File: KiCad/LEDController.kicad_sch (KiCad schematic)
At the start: 47 parts, among them J1 Conn_01x05, J2 UART, J3 JTAG, J5 USB_C_Receptacle_USB2.0_16P, J6 Conn_01x03, J7 VDD, J8 GND, J9 Conn_01x14, Q1 IRLZ44N, Q2 IRLZ44N, Q3 IRLZ44N, Q4 IRLZ44N, SW1 BOOT, SW2 EN, U2 ESP32-S3-WROOM-2, U3 TPS54202DDC

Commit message: .
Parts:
- C12, C14, C15, C5: footprint Capacitor_SMD:C_1210_3225Metric_Pad1.33x2.70mm_HandSolder -> Capacitor_SMD:C_0805_2012Metric_Pad1.18x1.45mm_HandSolder; LCSC (none) -> C33546007
- D1: footprint (none) -> LED_SMD:LED_0603_1608Metric_Pad1.05x0.95mm_HandSolder
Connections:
- net GPIO.6: now also U2.6 (GPIO6/TOUCH6/ADC1_CH5)
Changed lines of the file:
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@@
 		)
 	)
+	(global_label "GPIO.6"
+		(shape input)
+		(at 125.73 146.05 0)
+		(fields_autoplaced yes)
+		(effects
+			(font
+				(size 1.27 1.27)
+			)
+			(justify left)
+		)
+		(property "Intersheetrefs" "${INTERSHEET_REFS}"
+			(at 135.0048 146.05 0)
+			(effects
+				(font
+					(size 1.27 1.27)
+				)
+				(justify left)
+				(hide yes)
+			)
+		)
+	)
 	(global_label "UART.RX"
 		(shape input)
@@
 			)
 		)
-		(property "Footprint" "Capacitor_SMD:C_1210_3225Metric_Pad1.33x2.70mm_HandSolder"
+		(property "Footprint" "Capacitor_SMD:C_0805_2012Metric_Pad1.18x1.45mm_HandSolder"
 			(at 266.7 137.16 0)
 			(effects
@@
 			)
 		)
+		(property "LCSC" "C33546007"
+			(at 266.7 137.16 0)
+			(effects
+				(font
+					(size 1.27 1.27)
+				)
+				(hide yes)
+			)
+		)
 		(pin "1"
 		)
@@
 			)
 		)
-		(property "Footprint" "Capacitor_SMD:C_1210_3225Metric_Pad1.33x2.70mm_HandSolder"
+		(property "Footprint" "Capacitor_SMD:C_0805_2012Metric_Pad1.18x1.45mm_HandSolder"
 			(at 204.47 140.97 0)
 			(effects
@@
 			)
 		)
+		(property "LCSC" "C33546007"
+			(at 204.47 140.97 0)
+			(effects
+				(font
+					(size 1.27 1.27)
+				)
+				(hide yes)
+			)
+		)
 		(pin "1"
 		)
@@
 			)
 		)
-		(property "Footprint" "Capacitor_SMD:C_1210_3225Metric_Pad1.33x2.70mm_HandSolder"
+		(property "Footprint" "Capacitor_SMD:C_0805_2012Metric_Pad1.18x1.45mm_HandSolder"
 			(at 274.32 137.16 0)
 			(effects
@@
 			)
 		)
+		(property "LCSC" "C33546007"
+			(at 274.32 137.16 0)
+			(effects
+				(font
+					(size 1.27 1.27)
+				)
+				(hide yes)
+			)
+		)
 		(pin "1"
 		)
@@
 			)
 		)
-		(property "Footprint" "Capacitor_SMD:C_1210_3225Metric_Pad1.33x2.70mm_HandSolder"
+		(property "Footprint" "Capacitor_SMD:C_0805_2012Metric_Pad1.18x1.45mm_HandSolder"
 			(at 24.13 119.38 0)
 			(effects
@@
 			)
 		)
+		(property "LCSC" "C33546007"
+			(at 24.13 119.38 0)
+			(effects
+				(font
+					(size 1.27 1.27)
+				)
+				(hide yes)
+			)
+		)
 		(pin "2"
 		)
@@
 			)
 		)
-		(property "Footprint" ""
+		(property "Footprint" "LED_SMD:LED_0603_1608Metric_Pad1.05x0.95mm_HandSolder"
 			(at 128.27 90.17 0)
 			(effects

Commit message: .
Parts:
- added C6: 10u, Capacitor_SMD:C_0805_2012Metric_Pad1.18x1.45mm_HandSolder, symbol Device:C_Small
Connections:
- net +3.3V: now also C6.1
- net GND: now also C6.2
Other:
- moved on the sheet: C14, C15, J5, R12, R13, R14

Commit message: jlcpcb order
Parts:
- removed R10: 100k, Resistor_SMD:R_0805_2012Metric_Pad1.20x1.40mm_HandSolder, symbol Device:R_Small
- removed R11: 21.7995k, Resistor_SMD:R_0805_2012Metric_Pad1.20x1.40mm_HandSolder, symbol Device:R_Small
- added C12: 10u, Capacitor_SMD:C_0805_2012Metric_Pad1.18x1.45mm_HandSolder, symbol Device:C_Small
- C1, C2, C3: LCSC (none) -> C5137467
- C4: value 22u -> 10u; LCSC (none) -> C33546007
- C6: renamed from C10; LCSC (none) -> C5137467
- C7: renamed from C11; LCSC (none) -> C5137467
- L1: renamed from L2; value 15u -> 10u; LCSC (none) -> C5349663
- U1: renamed from U3; LCSC (none) -> C191884
- renumbered C14 to C10, C15 to C11, C12 to C8, C6 to C9, J2 to J1, J7 to J2, J8 to J3, J1 to J4, J6 to J5, J5 to J6, J9 to J7, J3 to J8, R12 to R10, R13 to R11, R14 to R12, R9 to R7, R7 to R9
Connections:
- net +3.3V: now also C12.1
- net GND: now also C12.2
- net GPIO.48: no longer names the net of U2.25 (GPIO48/SPICLK_N/SUBSPICLK_N_DIFF)
- no-connect marks 9 -> 11
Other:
- note added: "IRLB8721"
- note added: "verbessern"
- moved on the sheet: C10, C11, C3, C6, C7, C8, C9, L1, R10, R11, R12, U1

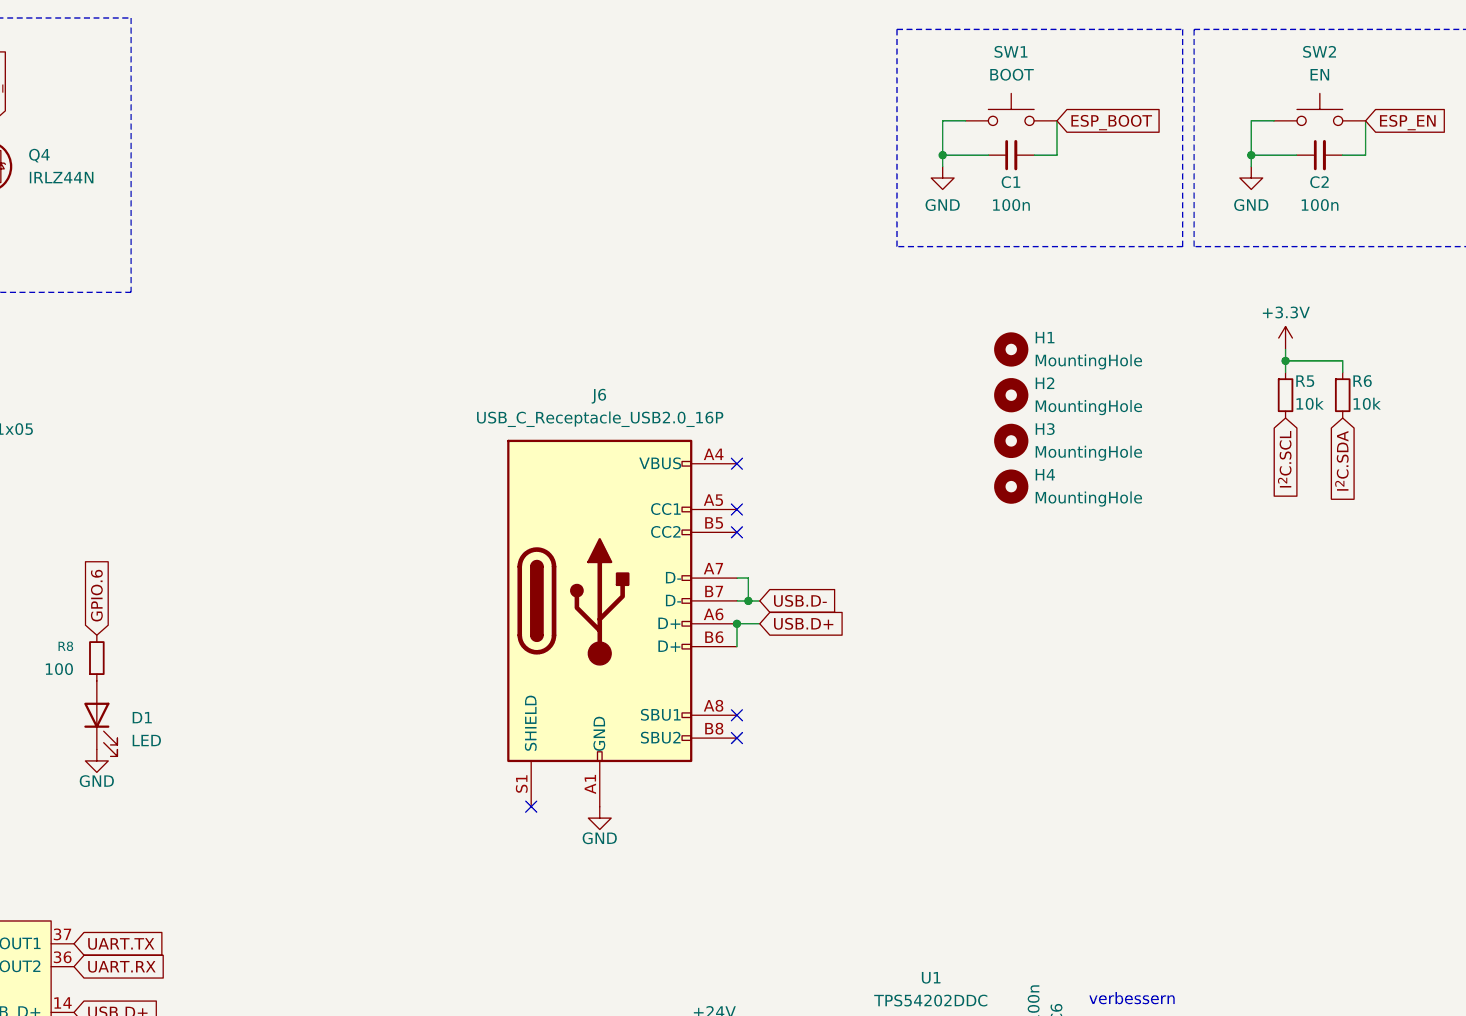
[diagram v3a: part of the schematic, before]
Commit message: add mains power
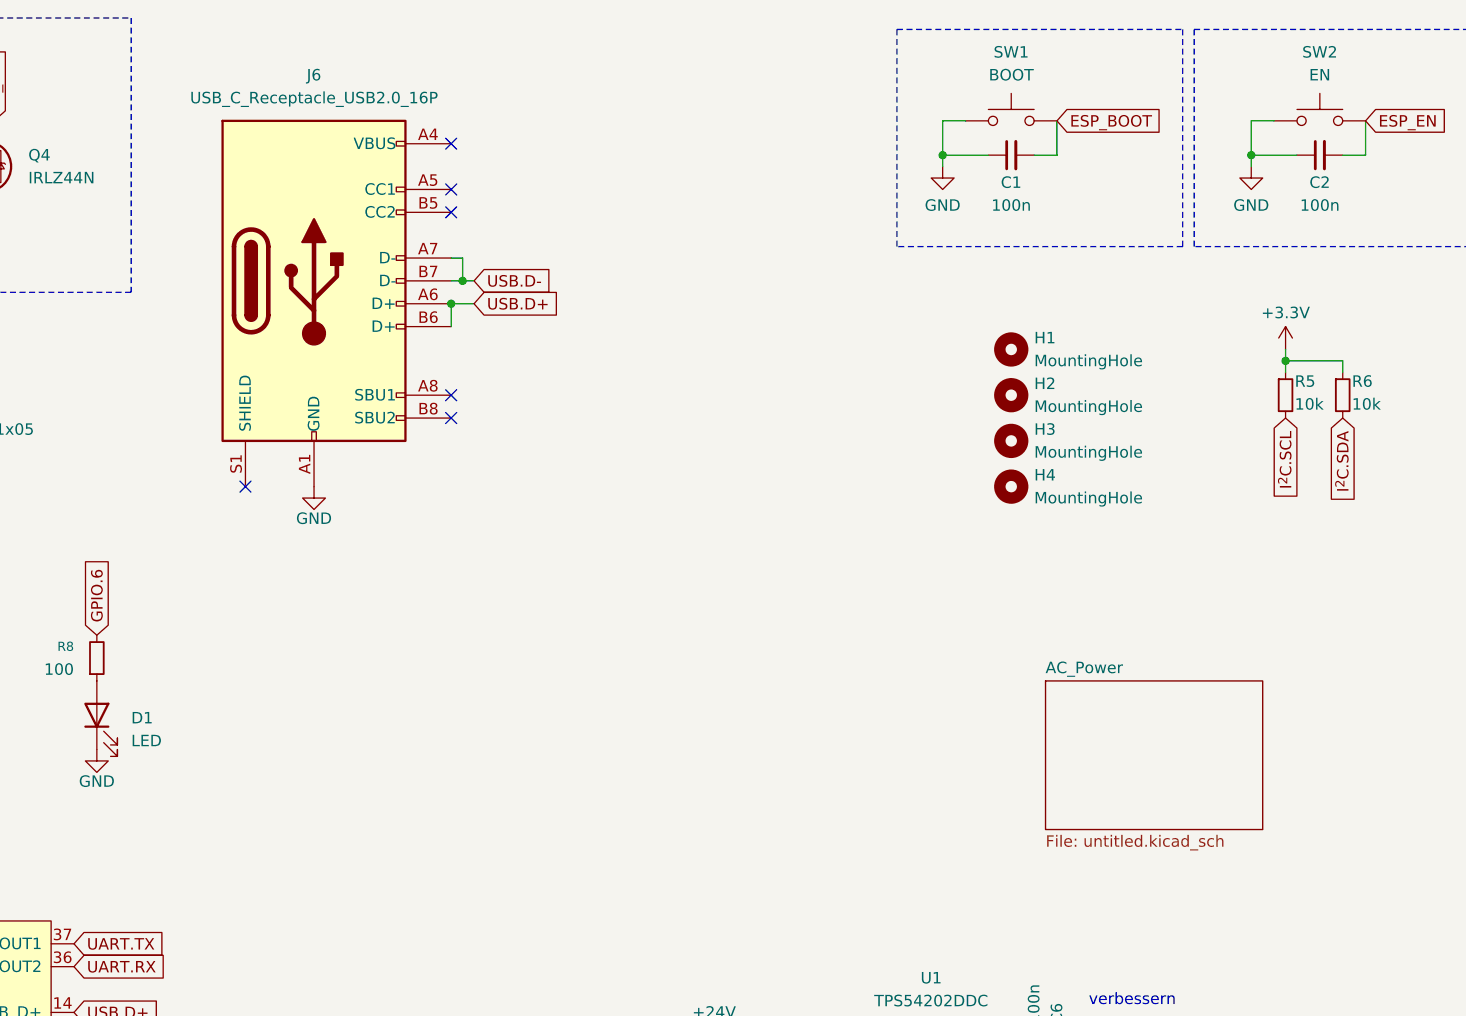
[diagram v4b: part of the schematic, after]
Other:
- added sheet AC_Power (untitled.kicad_sch)
- moved on the sheet: J6
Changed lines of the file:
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@@
 	)
 	(junction
-		(at 199.39 80.01)
+		(at 167.64 44.45)
 		(diameter 0)
 		(color 0 0 0 0)
@@
 	)
 	(junction
-		(at 200.66 77.47)
+		(at 168.91 41.91)
 		(diameter 0)
 		(color 0 0 0 0)
@@
 	)
 	(no_connect
-		(at 199.39 62.23)
+		(at 167.64 26.67)
 	)
 	(no_connect
-		(at 199.39 90.17)
+		(at 167.64 54.61)
 	)
 	(no_connect
@@
 	)
 	(no_connect
-		(at 199.39 67.31)
+		(at 167.64 31.75)
 	)
 	(no_connect
-		(at 199.39 92.71)
+		(at 167.64 57.15)
 	)
 	(no_connect
@@
 	)
 	(no_connect
-		(at 199.39 69.85)
+		(at 167.64 34.29)
 	)
 	(no_connect
-		(at 176.53 100.33)
+		(at 144.78 64.77)
 	)
 	(wire
@@
 	(wire
 		(pts
-			(xy 199.39 77.47) (xy 200.66 77.47)
+			(xy 167.64 41.91) (xy 168.91 41.91)
 		)
 		(stroke
@@
 	(wire
 		(pts
-			(xy 199.39 80.01) (xy 201.93 80.01)
+			(xy 167.64 44.45) (xy 170.18 44.45)
 		)
 		(stroke
@@
 	(wire
 		(pts
-			(xy 199.39 80.01) (xy 199.39 82.55)
+			(xy 167.64 44.45) (xy 167.64 46.99)
 		)
 		(stroke
@@
 	(wire
 		(pts
-			(xy 200.66 74.93) (xy 199.39 74.93)
+			(xy 168.91 39.37) (xy 167.64 39.37)
 		)
 		(stroke
@@
 	(wire
 		(pts
-			(xy 200.66 74.93) (xy 200.66 77.47)
+			(xy 168.91 39.37) (xy 168.91 41.91)
 		)
 		(stroke
@@
 	(wire
 		(pts
-			(xy 200.66 77.47) (xy 201.93 77.47)
+			(xy 168.91 41.91) (xy 170.18 41.91)
 		)
 		(stroke
@@
 	(global_label "USB.D+"
 		(shape input)
-		(at 201.93 80.01 0)
+		(at 170.18 44.45 0)
 		(fields_autoplaced yes)
 		(effects
@@
 		)
 		(property "Intersheetrefs" "${INTERSHEET_REFS}"
-			(at 212.1724 80.01 0)
+			(at 180.4224 44.45 0)
 			(effects
 				(font
@@
 	(global_label "USB.D-"
 		(shape input)
-		(at 201.93 77.47 0)
+		(at 170.18 41.91 0)
 		(fields_autoplaced yes)
 		(effects
@@
 		)
 		(property "Intersheetrefs" "${INTERSHEET_REFS}"
-			(at 212.1724 77.47 0)
+			(at 180.4224 41.91 0)
 			(effects
 				(font
@@
 	(symbol
 		(lib_id "Connector:USB_C_Receptacle_USB2.0_16P")
-		(at 184.15 77.47 0)
+		(at 152.4 41.91 0)
 		(unit 1)
 		(exclude_from_sim no)
@@
 		(fields_autoplaced yes)
 		(property "Reference" "J6"
-			(at 184.15 54.61 0)
+			(at 152.4 19.05 0)
 			(effects
 				(font
@@
 		)
 		(property "Value" "USB_C_Receptacle_USB2.0_16P"
-			(at 184.15 57.15 0)
+			(at 152.4 21.59 0)
 			(effects
 				(font
@@
 		)
 		(property "Footprint" "Connector_USB:USB_C_Receptacle_GCT_USB4105-xx-A_16P_TopMnt_Horizontal"
-			(at 187.96 77.47 0)
+			(at 156.21 41.91 0)
 			(effects
 				(font
@@
 		)
 		(property "Datasheet" "https://lcsc.com/datasheet/lcsc_datasheet_2505061156_SHOU-HAN-TYPE-C-16PIN-2MD-073_C2765186.pdf"
-			(at 187.96 77.47 0)
+			(at 156.21 41.91 0)
 			(effects
 				(font
@@
 		)
 		(property "Description" "USB 2.0-only 16P Type-C Receptacle connector"
-			(at 184.15 77.47 0)
+			(at 152.4 41.91 0)
 			(effects
 				(font
@@
 		)
 		(property "LCSC" "C2765186"
-			(at 184.15 77.47 0)
+			(at 152.4 41.91 0)
 			(effects
 				(font
@@
 	(symbol
 		(lib_id "power:GND")
-		(at 184.15 100.33 0)
+		(at 152.4 64.77 0)
 		(unit 1)
 		(exclude_from_sim no)
@@
 		(dnp no)
 		(property "Reference" "#PWR016"
-			(at 184.15 106.68 0)
+			(at 152.4 71.12 0)
 			(effects
 				(font
@@
 		)
 		(property "Value" "GND"
-			(at 184.15 103.886 0)
+			(at 152.4 68.326 0)
 			(effects
 				(font
@@
 		)
 		(property "Footprint" ""
-			(at 184.15 100.33 0)
+			(at 152.4 64.77 0)
 			(effects
 				(font
@@
 		)
 		(property "Datasheet" ""
-			(at 184.15 100.33 0)
+			(at 152.4 64.77 0)
 			(effects
 				(font
@@
 		)
 		(property "Description" "Power symbol creates a global label with name \"GND\" , ground"
-			(at 184.15 100.33 0)
+			(at 152.4 64.77 0)
 			(effects
 				(font
@@
 				)
 			)
+		)
+	)
+	(sheet
+		(at 233.68 86.36)
+		(size 24.13 16.51)
+		(exclude_from_sim no)
+		(in_bom yes)
+		(on_board yes)
+		(dnp no)
+		(fields_autoplaced yes)
+		(stroke
+			(width 0.1524)
+			(type solid)
+		)
+		(fill
+			(color 0 0 0 0.0000)
+		)
+		(property "Sheetname" "AC_Power"
+			(at 233.68 85.6484 0)
+			(effects
+				(font
+					(size 1.27 1.27)
+				)
+				(justify left bottom)
+			)
+		)
+		(property "Sheetfile" "untitled.kicad_sch"
+			(at 233.68 103.4546 0)
+			(effects
+				(font
+					(size 1.27 1.27)
+				)
+				(justify left top)
+			)
+		)
+		(instances
+			(project "LEDController"
+				(path "/4e4f96d2-86d5-4a03-8de9-74109a01887a"
+					(page "2")
+				)
+			)

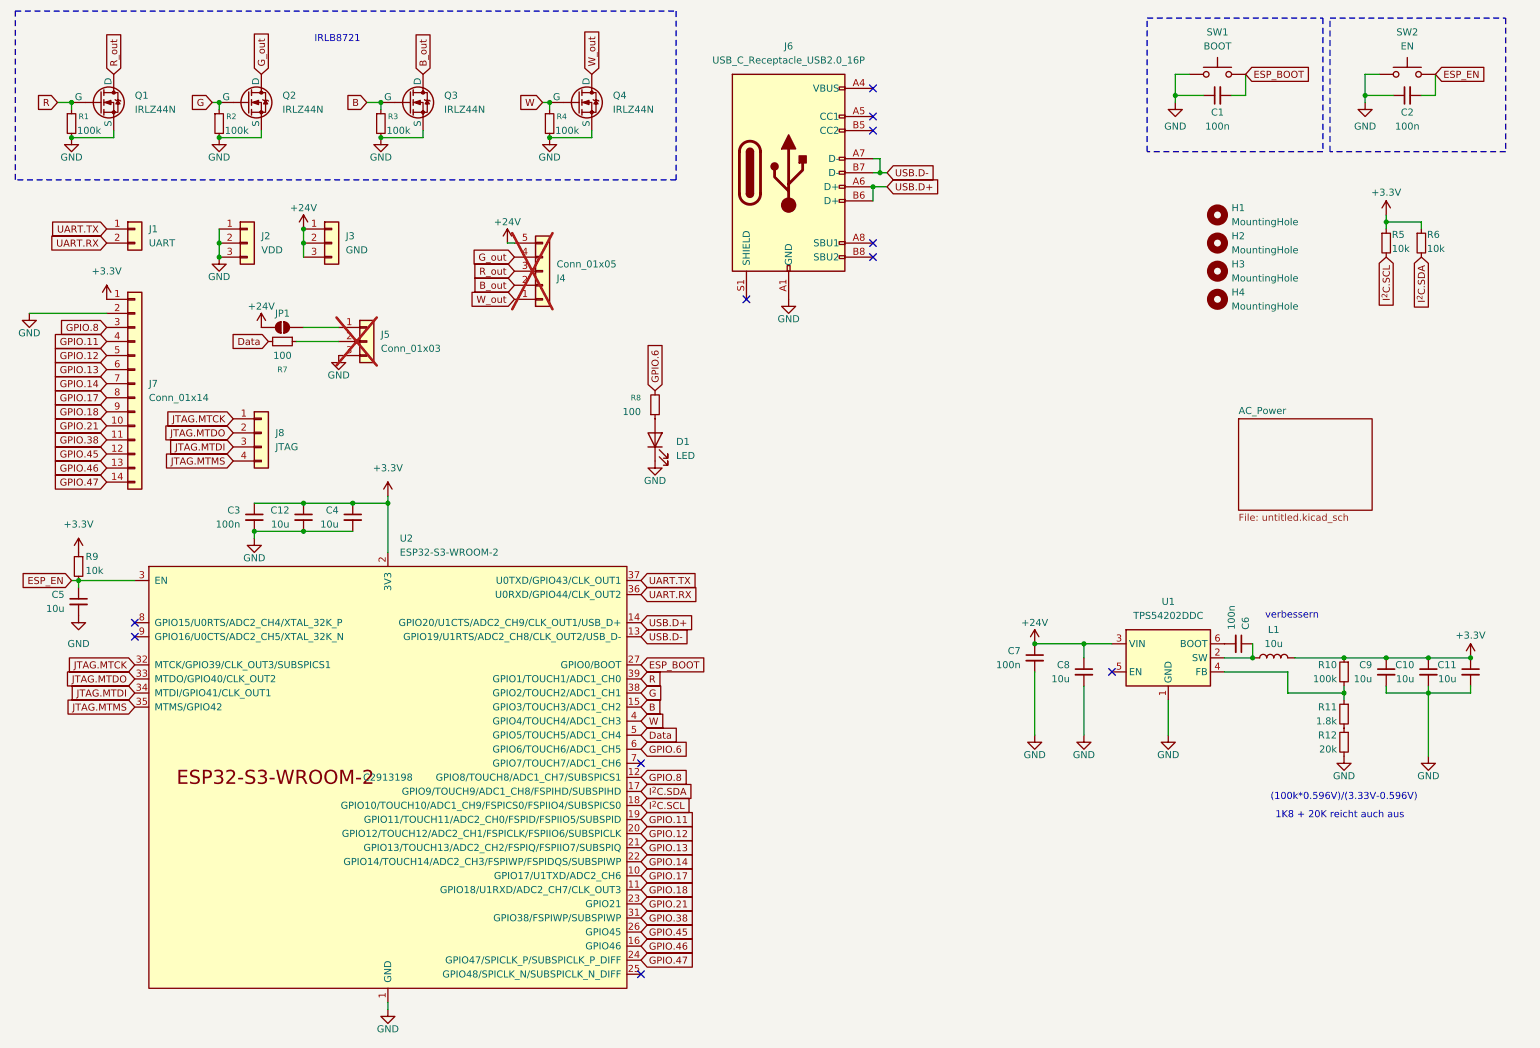
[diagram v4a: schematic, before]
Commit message: add 5v buck converter
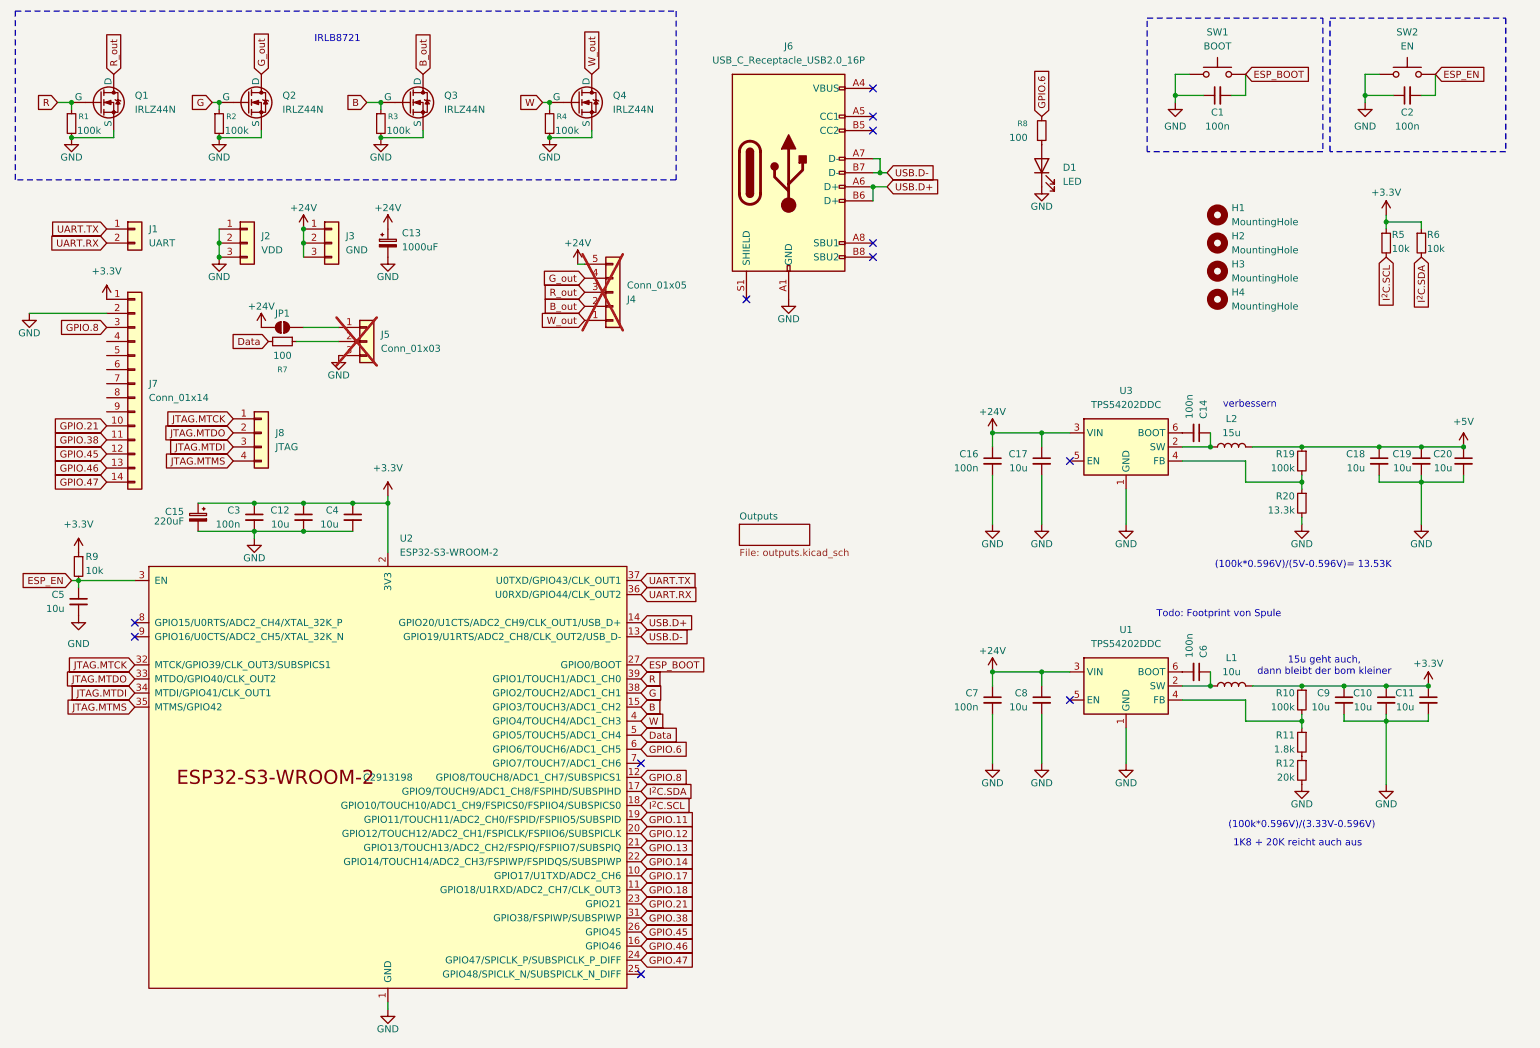
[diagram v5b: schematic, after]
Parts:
- added C13: 1000uF, symbol Device:C_Polarized_Small
- added C14, C16: 100n, Capacitor_SMD:C_0805_2012Metric_Pad1.18x1.45mm_HandSolder, symbol Device:C_Small
- added C15: 220uF, Capacitor_THT:CP_Radial_D8.0mm_P3.50mm, symbol Device:C_Polarized_Small
- added C17, C18, C19, C20: 10u, Capacitor_SMD:C_0805_2012Metric_Pad1.18x1.45mm_HandSolder, symbol Device:C_Small
- added L2: 15u, Inductor_SMD:L_APV_ANR4026, symbol Device:L
- added R19: 100k, Resistor_SMD:R_0805_2012Metric_Pad1.20x1.40mm_HandSolder, symbol Device:R_Small
- added R20: 13.3k, Resistor_SMD:R_0805_2012Metric_Pad1.20x1.40mm_HandSolder, symbol Device:R_Small
- added U3: TPS54202DDC, Package_TO_SOT_SMD:SOT-23-6, symbol Regulator_Switching:TPS54202DDC
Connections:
- net +24V: now also C13.1, C16.1, C17.1, U3.3 (VIN)
- net +3.3V: now also C15.1
- net GND: now also C13.2, C15.2, C16.2, C17.2, C18.2, C19.2, C20.2, R20.2, U3.1 (GND)
- net GPIO.11: no longer J7.4 (Pin_4)
- net GPIO.12: no longer J7.5 (Pin_5)
- net GPIO.13: no longer J7.6 (Pin_6)
- net GPIO.14: no longer J7.7 (Pin_7)
- net GPIO.17: no longer J7.8 (Pin_8)
- net GPIO.18: no longer J7.9 (Pin_9)
- new net: C14.1, L2.1, U3.2 (SW)
- new net: C14.2, U3.6 (BOOT)
- new net: R19.2, R20.1, U3.4 (FB)
- new net +5V: C18.1, C19.1, C20.1, L2.2, R19.1
- no-connect marks 11 -> 12
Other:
- removed sheet AC_Power
- added sheet Outputs (outputs.kicad_sch)
- note added: "(100k*0.596V)/(5V-0.596V)= 13.53K"
- note added: "15u geht auch, dann bleibt der bom kleiner"
- note added: "Todo: Footprint von Spule"
- moved on the sheet: C10, C11, C6, C7, C8, C9, D1, J4, L1, R10, R11, R12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
